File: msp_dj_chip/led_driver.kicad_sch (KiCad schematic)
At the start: 26 parts, among them J24 Conn_01x10_Socket, J7 Conn_01x10_Socket

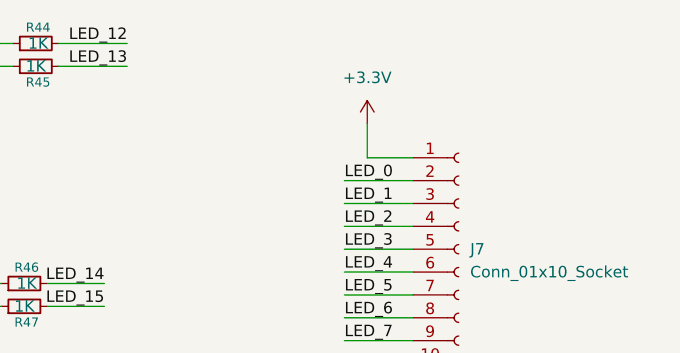
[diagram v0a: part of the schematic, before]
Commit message: adding back footprints and symbols
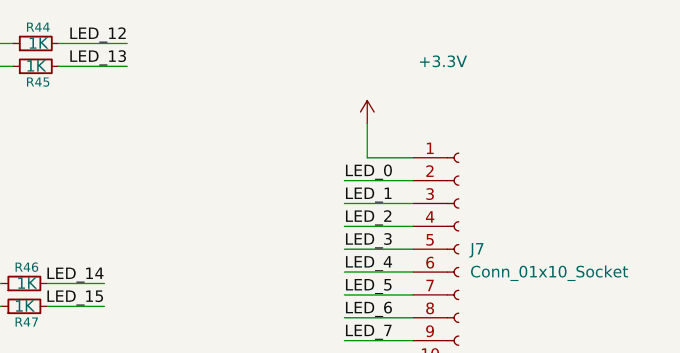
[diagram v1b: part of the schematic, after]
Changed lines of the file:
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@@
 		(on_board yes)
 		(dnp no)
-		(fields_autoplaced yes)
 		(property "Reference" "#PWR065"
 			(at 165.1 40.64 0)
@@
 		)
 		(property "Value" "+3.3V"
-			(at 165.1 31.75 0)
+			(at 173.482 29.972 0)
 			(effects
 				(font

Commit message: labeling ERC checking
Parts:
- renumbered J24 to J23, J7 to J24, R34 to R126, R35 to R127, R36 to R128, R37 to R129, R38 to R130, R39 to R131, R40 to R132, R41 to R133, R42 to R134, R43 to R135, R31 to R136, R32 to R137, R46 to R138, R47 to R139, R44 to R140, R45 to R141, U9 to U17, U10 to U18, U11 to U19, U12 to U20, U13 to U21, U7 to U22, U15 to U23, U14 to U24

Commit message: cleanup changes
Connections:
- net +3.3V renamed +3V3
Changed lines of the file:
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@@
 			)
 		)
-		(property "Value" "+3.3V"
-			(at 173.482 29.972 0)
+		(property "Value" "+3V3"
+			(at 165.1 32.004 0)
 			(effects
 				(font
@@
 			)
 		)
-		(property "Value" "+3.3V"
+		(property "Value" "+3V3"
 			(at 163.83 76.2 0)
 			(effects

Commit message: updating footprint assignments
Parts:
- R126, R127, R128, R129, R130, R131, R132, R133, R134, R135, R136, R137, R138, R139, R140, R141: footprint (none) -> Resistor_SMD:R_0603_1608Metric
- U17, U18, U19, U20, U21, U22, U23, U24: value ~ -> SSM6N7002KFU
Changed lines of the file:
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@@
 			)
 		)
-		(property "Value" "~"
+		(property "Value" "SSM6N7002KFU"
 			(at 49.53 49.53 0)
 			(effects
@@
 			)
 		)
-		(property "Footprint" ""
+		(property "Footprint" "Resistor_SMD:R_0603_1608Metric"
 			(at 128.27 30.48 0)
 			(effects
@@
 			)
 		)
-		(property "Value" "~"
+		(property "Value" "SSM6N7002KFU"
 			(at 49.53 76.2 0)
 			(effects
@@
 			)
 		)
-		(property "Footprint" ""
+		(property "Footprint" "Resistor_SMD:R_0603_1608Metric"
 			(at 127 57.15 0)
 			(effects
@@
 			)
 		)
-		(property "Value" "~"
+		(property "Value" "SSM6N7002KFU"
 			(at 113.03 22.86 0)
 			(effects
@@
 			)
 		)
-		(property "Footprint" ""
+		(property "Footprint" "Resistor_SMD:R_0603_1608Metric"
 			(at 64.77 81.28 0)
 			(effects
@@
 			)
 		)
-		(property "Value" "~"
+		(property "Value" "SSM6N7002KFU"
 			(at 50.8 22.86 0)
 			(effects
@@
 			)
 		)
-		(property "Footprint" ""
+		(property "Footprint" "Resistor_SMD:R_0603_1608Metric"
 			(at 64.77 83.82 0)
 			(effects
@@
 			)
 		)
-		(property "Value" "~"
+		(property "Value" "SSM6N7002KFU"
 			(at 49.53 104.14 0)
 			(effects
@@
 			)
 		)
-		(property "Footprint" ""
+		(property "Footprint" "Resistor_SMD:R_0603_1608Metric"
 			(at 64.77 111.76 0)
 			(effects
@@
 			)
 		)
-		(property "Value" "~"
+		(property "Value" "SSM6N7002KFU"
 			(at 111.76 49.53 0)
 			(effects
@@
 			)
 		)
-		(property "Footprint" ""
+		(property "Footprint" "Resistor_SMD:R_0603_1608Metric"
 			(at 64.77 57.15 0)
 			(effects
@@
 			)
 		)
-		(property "Footprint" ""
+		(property "Footprint" "Resistor_SMD:R_0603_1608Metric"
 			(at 64.77 134.62 0)
 			(effects
@@
 			)
 		)
-		(property "Footprint" ""
+		(property "Footprint" "Resistor_SMD:R_0603_1608Metric"
 			(at 64.77 109.22 0)
 			(effects
@@
 			)
 		)
-		(property "Footprint" ""
+		(property "Footprint" "Resistor_SMD:R_0603_1608Metric"
 			(at 66.04 27.94 0)
 			(effects
@@
 			)
 		)
-		(property "Footprint" ""
+		(property "Footprint" "Resistor_SMD:R_0603_1608Metric"
 			(at 66.04 30.48 0)
 			(effects
@@
 			)
 		)
-		(property "Footprint" ""
+		(property "Footprint" "Resistor_SMD:R_0603_1608Metric"
 			(at 64.77 54.61 0)
 			(effects
@@
 			)
 		)
-		(property "Value" "~"
+		(property "Value" "SSM6N7002KFU"
 			(at 49.53 129.54 0)
 			(effects
@@
 			)
 		)
-		(property "Footprint" ""
+		(property "Footprint" "Resistor_SMD:R_0603_1608Metric"
 			(at 64.77 137.16 0)
 			(effects
@@
 			)
 		)
-		(property "Footprint" ""
+		(property "Footprint" "Resistor_SMD:R_0603_1608Metric"
 			(at 128.27 27.94 0)
 			(effects
@@
 			)
 		)
-		(property "Footprint" ""
+		(property "Footprint" "Resistor_SMD:R_0603_1608Metric"
 			(at 64.77 160.02 0)
 			(effects
@@
 			)
 		)
-		(property "Footprint" ""
+		(property "Footprint" "Resistor_SMD:R_0603_1608Metric"
 			(at 127 54.61 0)
 			(effects
@@
 			)
 		)
-		(property "Value" "~"
+		(property "Value" "SSM6N7002KFU"
 			(at 49.53 152.4 0)
 			(effects
@@
 			)
 		)
-		(property "Footprint" ""
+		(property "Footprint" "Resistor_SMD:R_0603_1608Metric"
 			(at 64.77 157.48 0)
 			(effects

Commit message: more footprint assignments
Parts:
- J23, J24: footprint (none) -> project_footprints:CONN HEADER VERT 10POS 2MM
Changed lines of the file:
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@@
 			)
 		)
-		(property "Footprint" ""
+		(property "Footprint" "project_footprints:CONN HEADER VERT 10POS 2MM"
 			(at 173.99 95.25 0)
 			(effects
@@
 			)
 		)
-		(property "Footprint" ""
+		(property "Footprint" "project_footprints:CONN HEADER VERT 10POS 2MM"
 			(at 175.26 50.8 0)
 			(effects

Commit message: mosfet footprint assignments
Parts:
- U17, U18, U19, U20, U21, U22, U23, U24: footprint (none) -> project_footprints:MOSFET SSM6N7002KFU
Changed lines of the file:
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@@
 			)
 		)
-		(property "Footprint" ""
+		(property "Footprint" "project_footprints:MOSFET SSM6N7002KFU"
 			(at 53.34 58.42 0)
 			(effects
@@
 			)
 		)
-		(property "Footprint" ""
+		(property "Footprint" "project_footprints:MOSFET SSM6N7002KFU"
 			(at 53.34 85.09 0)
 			(effects
@@
 			)
 		)
-		(property "Footprint" ""
+		(property "Footprint" "project_footprints:MOSFET SSM6N7002KFU"
 			(at 116.84 31.75 0)
 			(effects
@@
 			)
 		)
-		(property "Footprint" ""
+		(property "Footprint" "project_footprints:MOSFET SSM6N7002KFU"
 			(at 54.61 31.75 0)
 			(effects
@@
 			)
 		)
-		(property "Footprint" ""
+		(property "Footprint" "project_footprints:MOSFET SSM6N7002KFU"
 			(at 53.34 113.03 0)
 			(effects
@@
 			)
 		)
-		(property "Footprint" ""
+		(property "Footprint" "project_footprints:MOSFET SSM6N7002KFU"
 			(at 115.57 58.42 0)
 			(effects
@@
 			)
 		)
-		(property "Footprint" ""
+		(property "Footprint" "project_footprints:MOSFET SSM6N7002KFU"
 			(at 53.34 138.43 0)
 			(effects
@@
 			)
 		)
-		(property "Footprint" ""
+		(property "Footprint" "project_footprints:MOSFET SSM6N7002KFU"
 			(at 53.34 161.29 0)
 			(effects
